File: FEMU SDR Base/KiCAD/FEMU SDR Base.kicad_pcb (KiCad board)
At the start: 4 copper layers, 164.8 x 164.8 mm, 98 parts, among them M1 M1, M10 M1, M11 M1, M12 M1, M13 M1, M14 M1, M15 M1, M16 M1, M2 M1, M3 M1, M4 M1, M5 M1, M6 M1, M7 M1, M8 M1, M9 M1, P1 Battery, P10 PWM2, P11 PWM3, P12 PWM4, P13 PWM1, P14 PWM2, P15 PWM3, P16 PWM4, P17 12V, P18 GND, P19 12V, P2 SDR_Shield_1, P20 GND, P21 SDR0, P22 SDR1, P27 PWM0, P28 PWM5, P29 PWM6, P3 SDR_Shield_2, P30 PWM7, P31 PWM0, P32 PWM5, P33 PWM6, P34 PWM7, P35 Battery, P36 RPi, P37 PXH, P38 Rx, P4 12V, P5 GND, P6 12V, P7 GND, P8 Raspi_Power_Shield, P9 PWM1, U1 TPS562209, U2 LP38858-LDO, U3 LP38858-LDO, U4 LM1117, U5 LM1117

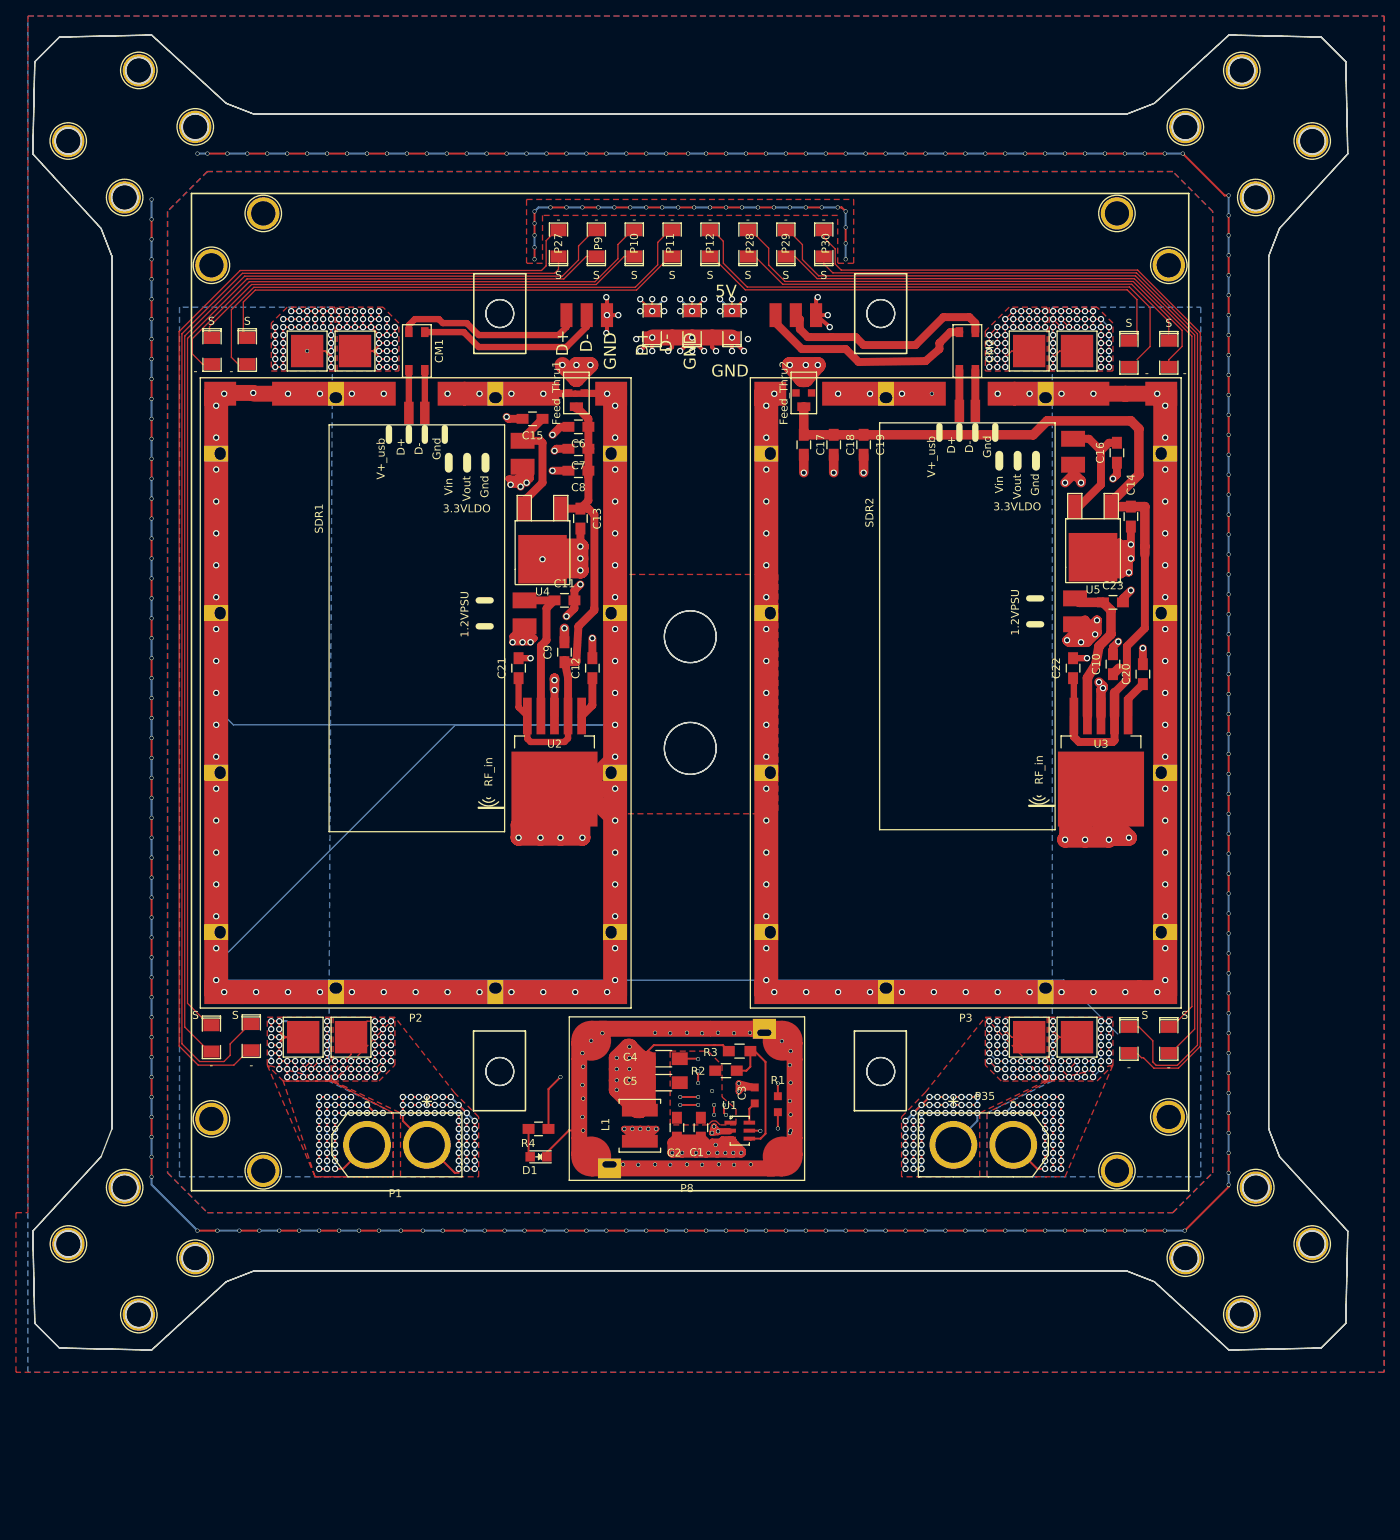
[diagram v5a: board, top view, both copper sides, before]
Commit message: Added back silkscreen, fixed issues and added mounting holes
Signed-off-by: hardiepienaar <hardiepienaar@gmail.com>
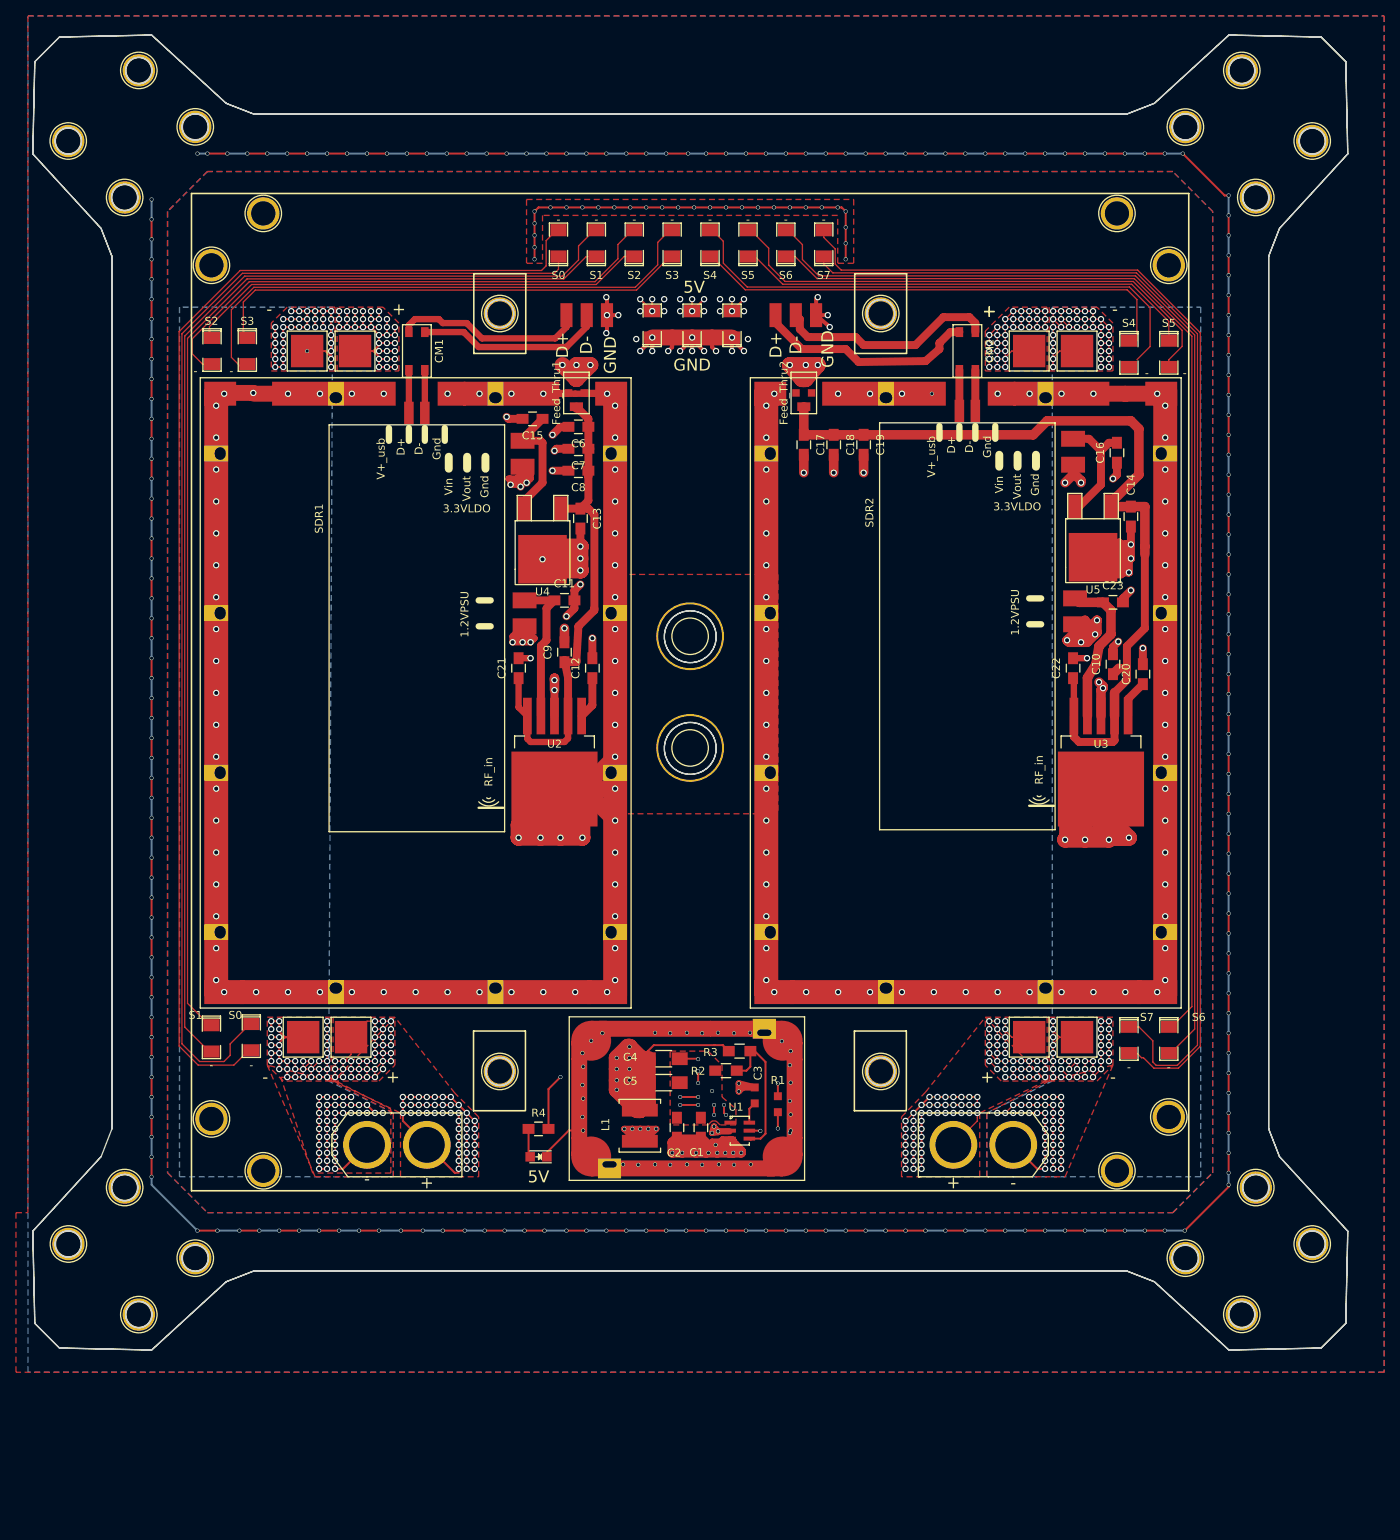
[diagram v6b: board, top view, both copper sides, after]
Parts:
- added M17: 1pin, SMAMount, F.Cu at (84.5, 77.5)
- added M18: 1pin, SMAMount, F.Cu at (84.5, 91.5)
- added REF**: 1pin, Connect:1pin, F.Cu at (108.4, 132.1)
- added REF**: 1pin, Connect:1pin, F.Cu at (60.6, 132.1)
- added REF**: 1pin, Connect:1pin, F.Cu at (108.4, 37.0)
- added REF**: 1pin, Connect:1pin, F.Cu at (60.6, 37.0)
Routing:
- net GND: track 2008.4 -> 1802.6 mm, vias 687 -> 678
- net +12V: track 356.6 -> 350.6 mm, vias 241 -> 237
- net (no net): track 0.00 -> 6.00 mm, vias 0 -> 13
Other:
- board text added: "3.0"
- board text added: "=>"
- board text added: "Finish SDR layouts (Antheun) Add MESA logo Move usb terminal away from shield Fix section on sheild that is not grounded"
- board text added: "May 2016"
- board text added: "RF goes here ->"
- board text added: "Rev: 1"
- board text added: "S0"
- board text added: "S1"
- board text added: "S2"
- board text added: "S3"
- board text added: "S4"
- board text added: "S5"
- board text added: "S6"
- board text added: "S7"
- board text added: "This way forward"
- board text added: "fEMu"
- board text removed: "Connect 5V line (Antheun) Add feedthroughs (Antheun) Add usb isolation (Antheun) Finish SDR layouts (Antheun) Add MESA logo Add FEMU logo Add Description Add Rev and date Add Sneaky signitures"
- board text removed: "S"

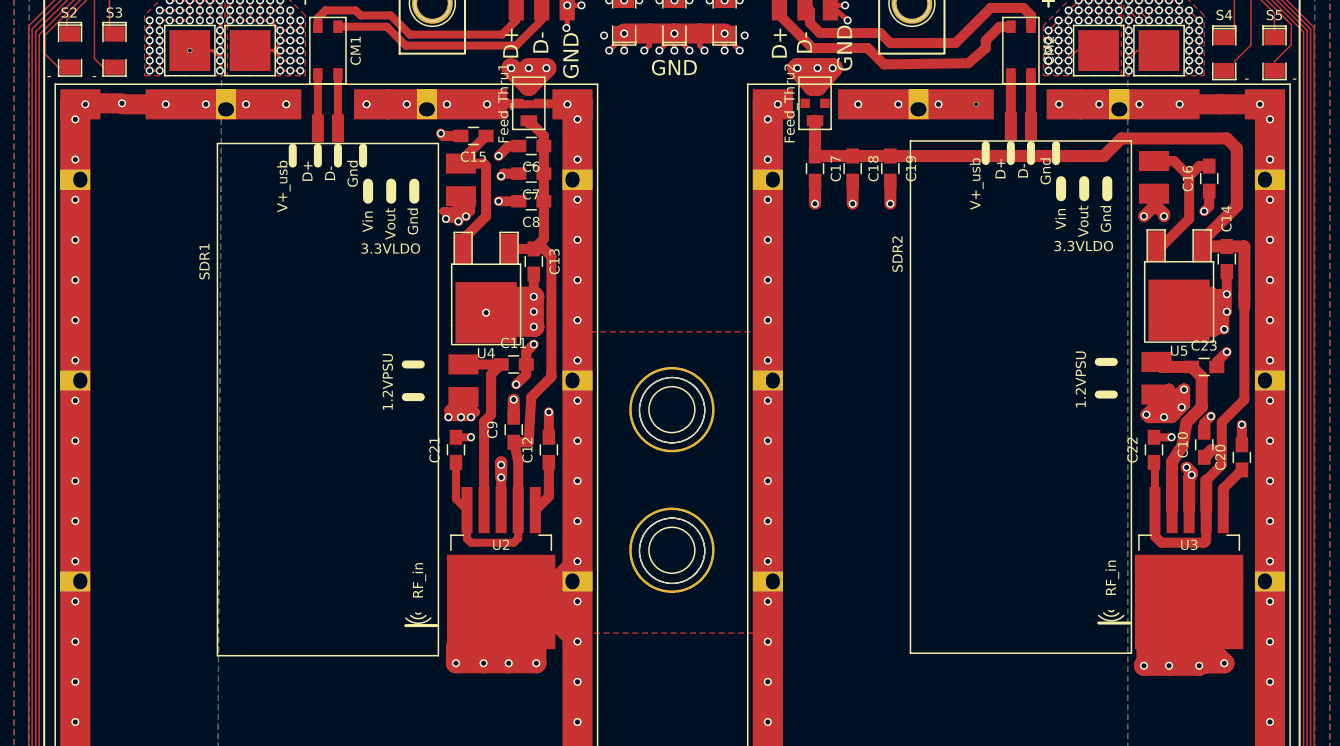
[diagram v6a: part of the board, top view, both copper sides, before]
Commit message: Last Tasks: Moved SDR pads away from shields, layouts refined, added FMask pads to traces for continuous shield contact, added MPS LOGO... Final checks TODO
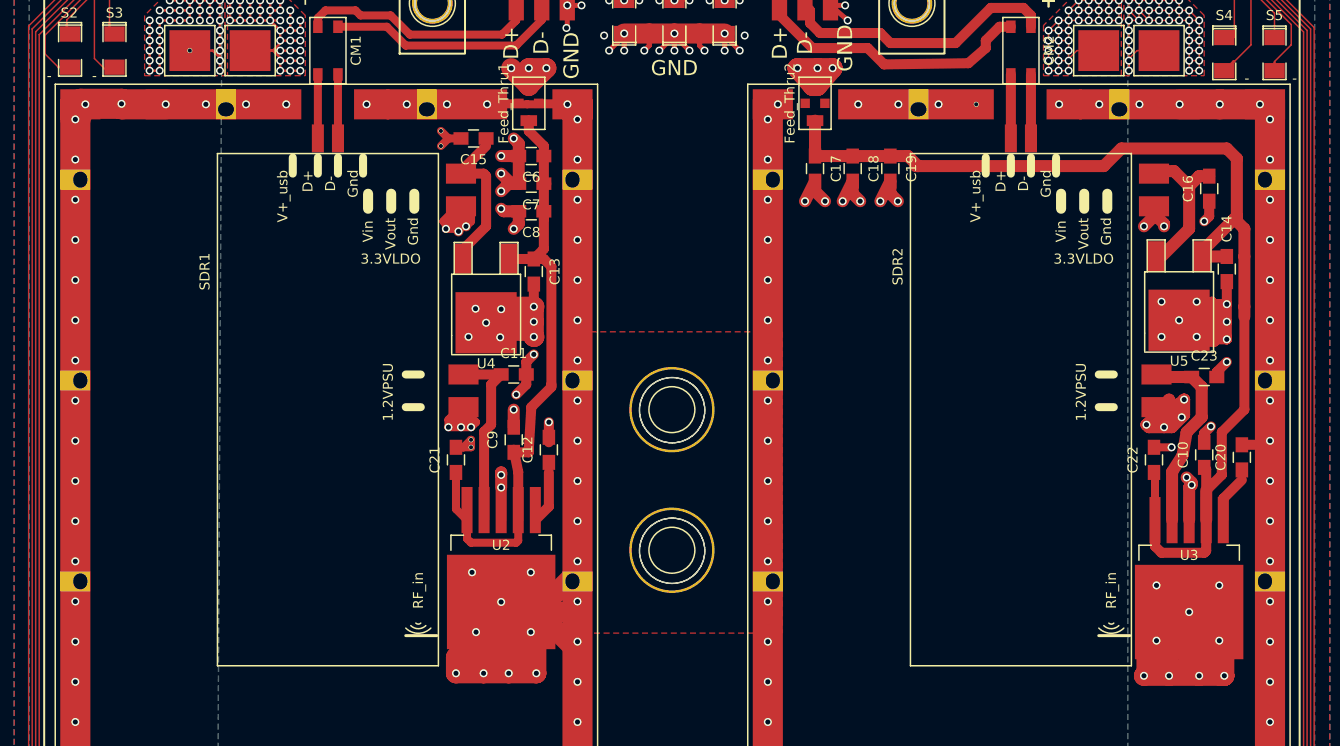
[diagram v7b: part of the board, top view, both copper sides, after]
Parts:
- added G***: LOGO, Misc footprints:MPS_LOGO_Flipped, B.SilkS at (94.1, 66.5)
- moved SDR2 1.25 mm to (108.2, 103.0)
- moved C10 1.00 mm to (137.5, 82.0)
- moved C11 1.00 mm to (68.8, 74.0)
- moved C13 1.00 mm to (70.8, 63.8)
- moved C14 1.00 mm to (139.8, 63.5)
- moved C16 1.00 mm to (138.0, 55.5)
- moved C21 1.00 mm to (63.0, 82.5)
- moved C22 1.00 mm to (132.5, 82.5)
- moved C23 1.00 mm to (137.5, 74.2)
- moved C6 1.00 mm to (70.5, 52.2)
- moved C7 1.00 mm to (70.5, 55.0)
- moved C8 1.00 mm to (70.5, 57.8)
- moved C9 1.00 mm to (68.8, 80.5)
- moved SDR1 1.00 mm to (39.2, 103.0)
- moved U3 1.00 mm to (136.0, 88.5)
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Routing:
- net GND: track 1802.6 -> 1965.7 mm, vias 678 -> 705
- net /5V_S1: track 107.8 -> 114.2 mm
- net Net-(SDR1-PadGND): track 29.5 -> 31.6 mm
- net Net-(P12-Pad2): track 68.0 -> 69.4 mm
- net /5V_S0: track 64.3 -> 65.4 mm
- net /D-_S0: track 5.38 -> 6.38 mm
- net /D+_S0: track 5.38 -> 6.38 mm
- net Net-(P28-Pad2): track 66.1 -> 66.9 mm
- net /3V3_S0: track 14.8 -> 15.6 mm
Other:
- board text removed: "Finish SDR layouts (Antheun) Add MESA logo Move usb terminal away from shield Fix section on sheild that is not grounded"
